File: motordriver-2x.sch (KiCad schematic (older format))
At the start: 442 parts

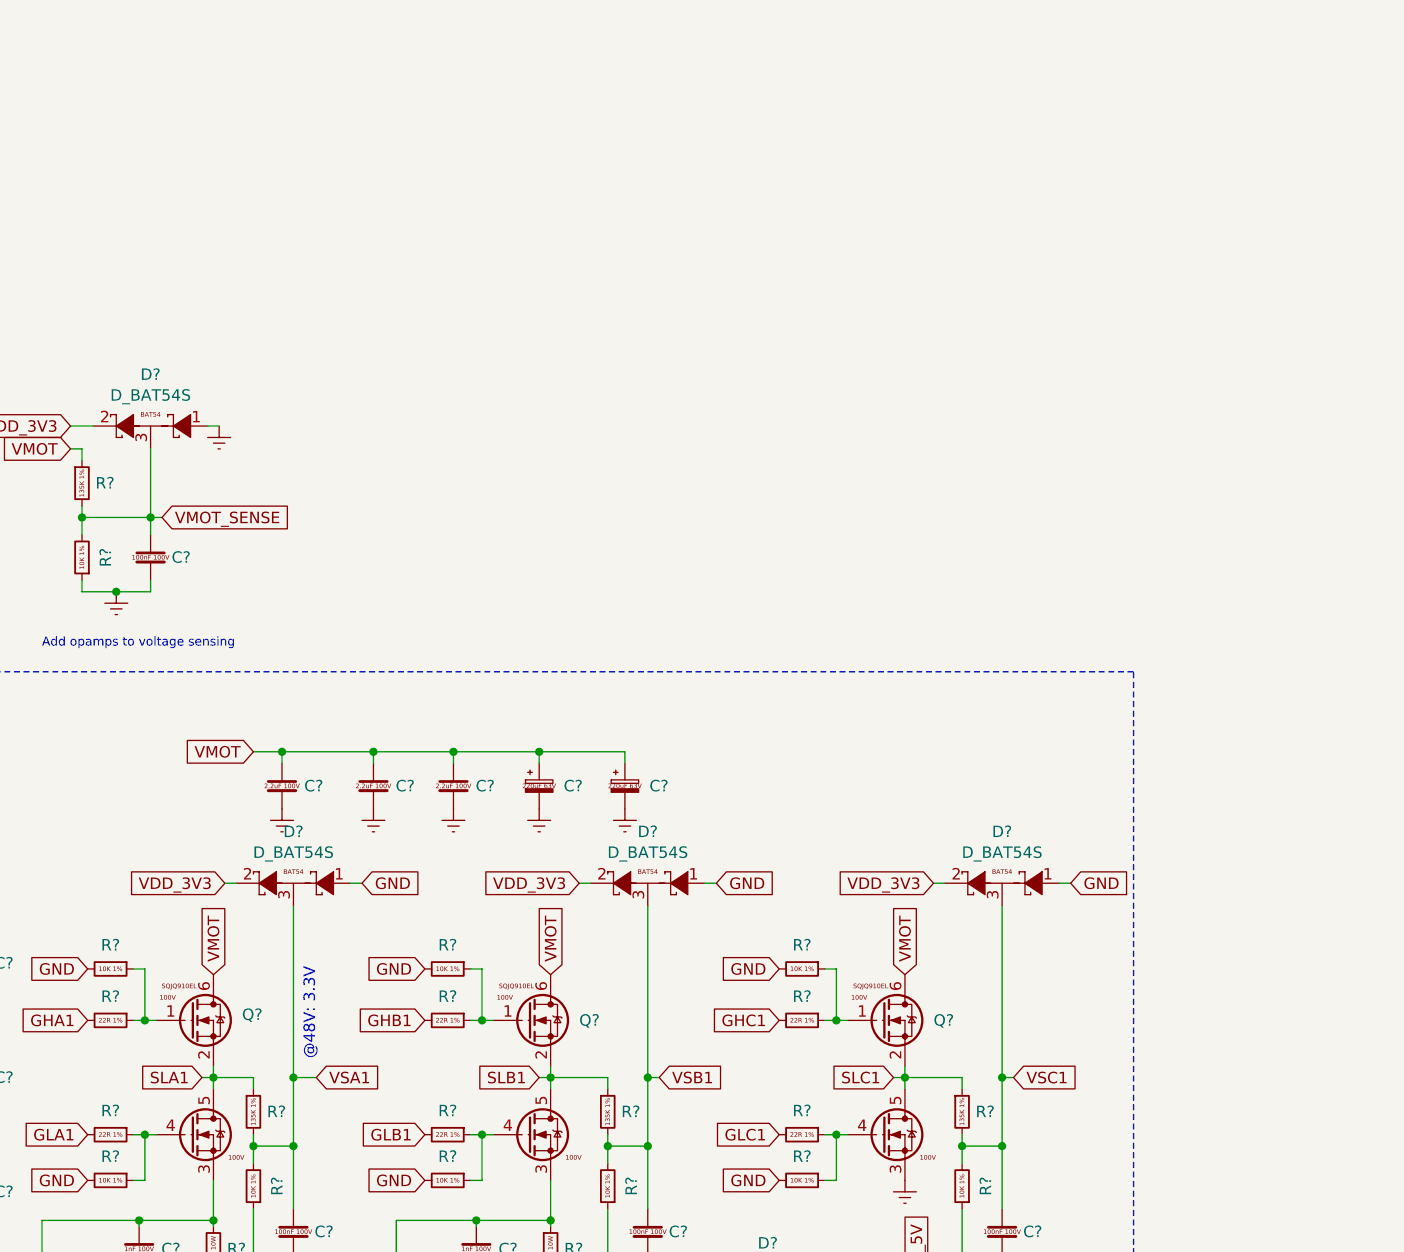
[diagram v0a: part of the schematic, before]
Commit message: add opamps to voltage sensing
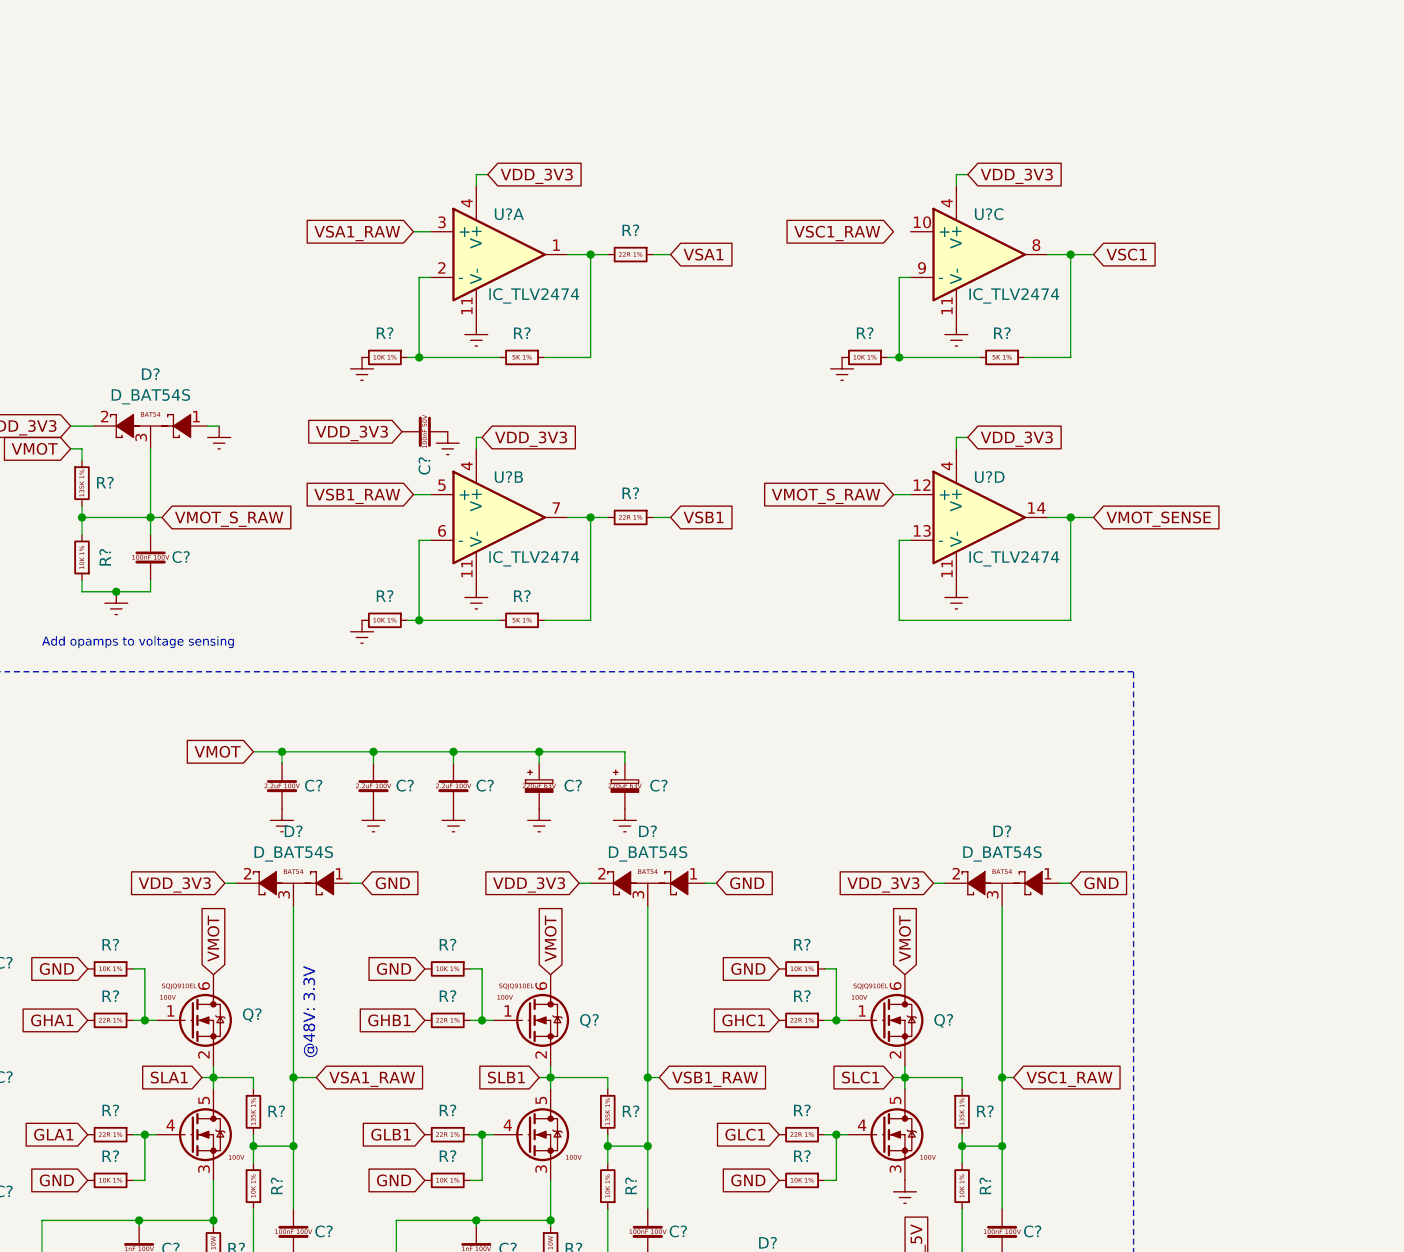
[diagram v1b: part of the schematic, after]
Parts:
- added C?: CAP_100nF_50V_0402, Capacitor_SMD:C_0402_1005Metric, symbol SwEmb:CAP_100nF_50V_0402
- added R? (x2): RES_22R_1%_0402, Resistor_SMD:R_0402_1005Metric, symbol SwEmb:RES_22R_1%_0402
- added R? (x3): RES_5K_1%_0402, Resistor_SMD:R_0402_1005Metric, symbol SwEmb:RES_5K_1%_0402
- added R? (x3): RES_10K_1%_0402, Resistor_SMD:R_0402_1005Metric, symbol SwEmb:RES_10K_1%_0402
- added U? (x4): IC_TLV2474, Package_SO:SOIC-14_3.9x8.7mm_P1.27mm, symbol SwEmb:IC_TLV2474
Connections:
- net labels added: VMOT_S_RAW, VSA1_RAW, VSB1_RAW, VSC1_RAW
- wire segments 1434 -> 1477

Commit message: add preamp for voltage sensing and add UEXT
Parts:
- added C?: CAP_100nF_50V_0402, Capacitor_SMD:C_0402_1005Metric, symbol SwEmb:CAP_100nF_50V_0402
- added C?: CAP_22uF_10V_0805, Capacitor_SMD:C_0805_2012Metric, symbol SwEmb:CAP_22uF_10V_0805
- added D?: D_MM3Z3V3B, Diode_SMD:D_SOD-323F, symbol SwEmb:D_MM3Z3V3B
- added P?: CONN_UEXT, Connector_PinSocket_2.54mm:PinSocket_2x05_P2.54mm_Vertical, symbol SwEmb:CONN_UEXT
- added R? (x19): RES_10K_1%_0402, Resistor_SMD:R_0402_1005Metric, symbol SwEmb:RES_10K_1%_0402
- added R? (x2): RES_22R_1%_0402, Resistor_SMD:R_0402_1005Metric, symbol SwEmb:RES_22R_1%_0402
- added R? (x3): RES_5K_1%_0402, Resistor_SMD:R_0402_1005Metric, symbol SwEmb:RES_5K_1%_0402
- added U? (x4): IC_TLV2474, Package_SO:SOIC-14_3.9x8.7mm_P1.27mm, symbol SwEmb:IC_TLV2474
- added U?: IC_TLV5533, Package_TO_SOT_SMD:SOT-23-5, symbol SwEmb:IC_TLV5533
- R?: symbol SwEmb:RES_10K_1%_0402 -> SwEmb:RES_5K_1%_0402
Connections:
- net labels added: UEXT_CS, UEXT_MISO, UEXT_MOSI, UEXT_PWEN, UEXT_RX, UEXT_SCK, UEXT_SCL, UEXT_SDA, UEXT_TX, VSA2_RAW, VSB2_RAW, VSC2_RAW
- wire segments 1477 -> 1586
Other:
- note added: "Back-EMF ADC Pre-Amp w/ offset"
- note removed: "Add opamps to voltage sensing"
- moved on the sheet: C?, D?, R?, U?, U?A, U?B, U?C, U?D

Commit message: add gpio and connect most pins
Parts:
- removed D?: D_BAT54S, Package_TO_SOT_SMD:SOT-23, symbol SwEmb:D_BAT54S
- added C? (x2): CAP_100nF_50V_0402, Capacitor_SMD:C_0402_1005Metric, symbol SwEmb:CAP_100nF_50V_0402
- added J?: USB_B_Micro, Connector_USB:USB_Micro-B_GCT_USB3076-30-A, symbol SwEmb:USB_B_Micro
- added R? (x2): RES_22R_1%_0402, Resistor_SMD:R_0402_1005Metric, symbol SwEmb:RES_22R_1%_0402
- added U?: IC_USBLC6-2, Package_TO_SOT_SMD:SOT-23-6, symbol SwEmb:IC_USBLC6-2
- added U? (x2): IC_MCP23S17, symbol SwEmb:IC_MCP23S17
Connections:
- net labels added: GPEX0, GPEX1, GPEX2, GPEX3, GPEX4, GPEX5, GPEX6, GPEX7, GPEX_CS, GPEX_INTA, GPEX_INTB, GPEX_RESET, GPIO_CS, GPIO_INTA, GPIO_INTB, GPIO_MISO, GPIO_MOSI, GPIO_RESET, GPIO_SCK, LCD_D4, LCD_D5, LCD_D6, LCD_D7, LCD_EN, LCD_MDATA, LCD_READ, LCD_VO, USB_5V, USB_N, USB_P
- wire segments 1586 -> 1617
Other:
- note added: "Check addresses"
- moved on the sheet: P?

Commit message: update schematic
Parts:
- removed C? (x2): CAP_100nF_50V_0402, Capacitor_SMD:C_0402_1005Metric, symbol SwEmb:CAP_100nF_50V_0402
- removed U?: IC_TXS0108, Package_SO:TSSOP-20_4.4x6.5mm_P0.65mm, symbol SwEmb:IC_TXS0108
- added C? (x5): CAP_2.2uF_16V_0402, Capacitor_SMD:C_0402_1005Metric, symbol SwEmb:CAP_2.2uF_16V_0402
- added C? (x2): CAP_100nF_50V_0402, Capacitor_SMD:C_0402_1005Metric, symbol SwEmb:CAP_100nF_50V_0402
- added P? (x8): CONN_SWITCH, TerminalBlock_4Ucon:TerminalBlock_4Ucon_1x02_P3.50mm_Horizontal, symbol SwEmb:CONN_LED
- added R?: RES_470R_1%_0402, Resistor_SMD:R_0402_1005Metric, symbol SwEmb:RES_470R_1%_0402
- added R? (x8): RES_0R_0402, Resistor_SMD:R_0402_1005Metric, symbol SwEmb:RES_0R_0402
- added U?: IC_LP55231, Package_DFN_QFN:WQFN-24-1EP_4x4mm_P0.5mm_EP2.7x2.7mm, symbol SwEmb:IC_LP55231
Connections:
- net labels added: BLED_EN, BLED_INT, BLED_SCL, BLED_SDA, LCD_D0, LCD_D1, LCD_D2, LCD_D3, LCD_LED
- net labels removed: GPEX0, GPEX1, GPEX2, GPEX3, GPEX4, GPEX5, GPEX6, GPEX7
- wire segments 1617 -> 1703
- no-connect marks 57 -> 53
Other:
- note added: "Button LEDs"
- note added: "LCD"
- note added: "Sw/Ctrl IO"
- note added: "UEXT"
- note removed: "GP/Expansion IO"
- note removed: "Implement industrial digital inputs with 30v tolerance"
- moved on the sheet: C?, P?, U?

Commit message: update annotated schematic
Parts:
- added C70: CAP_100nF_50V_0402, Capacitor_SMD:C_0402_1005Metric, symbol SwEmb:CAP_100nF_50V_0402
- added R39, R55, R61, R65: RES_10mOhm_1%, Resistor_SMD:R_0805_2012Metric, symbol SwEmb:RES_10mOhm_1%
- added R76: RES_22R_1%_0402, Resistor_SMD:R_0402_1005Metric, symbol SwEmb:RES_22R_1%_0402
- added TP10, TP17, TP20, TP21, TP22: Test_Point, TestPoint:TestPoint_Pad_1.0x1.0mm, symbol SwEmb:Test_Point
- added unit 1 of U26
- gave numbers to parts that had none: 503
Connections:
- net BLED_SCL is gone; now on net AP_SCL1: U21.9 (SCL)
- net BLED_SDA is gone; now on net AP_SDA1: U21.8 (SDA)
- net AINPWEN: now also U12.12 (PF2/FMC_A2/I2C2_SMBA)
- net BLED_EN: now also U12.58 (PE7/FMC_D4/FMC_DA4/TIM1_ETR/UART7_RX)
- net BLED_INT: now also U12.67 (PE14/FMC_D11/FMC_DA11/LTDC_CLK/SPI4_MOSI/TIM1_CH4)
- net ENCPWEN1: now also U12.70 (ADC1_EXTI11/ADC2_EXTI11/ADC3_EXTI11/ETH_TX_EN/I2C2_SDA/LTDC_G5/TIM2_CH4/USART3_RX/USB_OTG_HS_ULPI_D4/PB11)
- net ENCPWEN2: now also U12.69 (ETH_RX_ER/I2C2_SCL/I2S2_CK/LTDC_G4/SPI2_SCK/TIM2_CH3/USART3_TX/USB_OTG_HS_ULPI_D3/PB10)
- net GNDREF: now also S2.1 (A1), S2.2 (B1), S2.3 (C1), S2.4 (D1), C70.1, U26.11 (V-)
- net GPEX_CS: now also U12.19 (PF7/ADC3_IN5/FMC_NREG/SAI1_MCLK_B/SPI5_SCK/TIM11_CH1/UART7_TX)
- net GPEX_INTA: now also U12.21 (PF9/ADC3_IN7/DAC_EXTI9/FMC_CD/SAI1_FS_B/SPI5_MOSI/TIM14_CH1)
- net GPEX_INTB: now also U12.22 (PF10/ADC3_IN8/DCMI_D11/FMC_INTR/LTDC_DE)
- net GPEX_RESET: now also U12.20 (PF8/ADC3_IN6/FMC_NIOWR/SAI1_SCK_B/SPI5_MISO/TIM13_CH1)
- net USB_5V: now also R61.2; no longer U22.1 (IN)
- net VDD_3V3: now also C70.2, R65.1, TP22.1, U26.4 (V+); no longer C58.1, U22.5 (OUT)
- net VMOT: now also R39.2, TP10.1; no longer TP11.1, U14.2 (VIN)
- net VMOT_SENSE: now also R76.1
- net VSC1: now also U33.14; no longer U33.8
- net VSC2: now also U35.1; no longer U35.8
- net at S2.5 (D2): now also U13.28 (PA7)
- net at S2.6 (C2): now also U13.27 (PA6)
- net at S2.7 (B2): now also U13.26 (PA5)
- net at S2.8 (A2): now also U13.25 (PA4)
- net at C45.1, P23.1 (VCC), TP16.1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: now also R55.2; no longer C38.1, D14.1 (K), L1.2, R48.1
- net at R134.1, R135.2: now also U33.10 (+); no longer U33.5 (+)
- net at R136.1, R154.2: now also U33.9 (-); no longer U33.6 (-)
- net at R154.1, R162.2: now also U33.8; no longer U33.7
- net at R180.1, R181.2: now also U35.3 (+); no longer U35.10 (+)
- net at R182.1, R194.2: now also U35.2 (-); no longer U35.9 (-)
- net at R90.1, R91.2: now also U26.10 (+); no longer U26.12 (+)
- net at R135.1, R181.1, R98.1: now also U26.8, U26.9 (-); no longer U26.13 (-), U26.14
- net at R111.1, R121.2: now also U26.14; no longer U26.1
- net at R111.2, R96.1: now also U26.13 (-); no longer U26.2 (-)
- net at R94.1, R95.2: now also U26.12 (+); no longer U26.3 (+)
- net at R177.1, R178.2: now also U33.12 (+); no longer U33.10 (+)
- net at R179.1, R193.2: now also U33.13 (-); no longer U33.9 (-)
- net at R88.1, R89.2: now also U26.5 (+); no longer U26.12 (+)
- net at R132.1, R178.1, R95.1: now also U26.6 (-), U26.7; no longer U26.13 (-), U26.14
- net VMOT_S_RAW: no longer names the net of C63.1, D17.3, R68.2, R69.2
- net VMOT_S_RAW: now also U26.3 (+)
- new net: R39.1, TP11.1, U14.2 (VIN)
- new net: C38.1, D14.1 (K), L1.2, R48.1, R55.1, TP17.1
- new net: R61.1, TP20.1, U22.1 (IN)
- new net: C58.1, R65.2, TP21.1, U22.5 (OUT)
- new net: R76.2, U26.1, U26.2 (-)
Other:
- note added: "EtherCAT"
- note added: "GPIO"
- note added: "Supply Voltage Sense"
- note added: "USB"
- note removed: "150mA"
- note removed: "Add current sensing to each supply"
- note removed: "Sw/Ctrl IO"
- note removed: "Use extra inputs for HALL?\nAdd possibility to bypass"
- moved on the sheet: C102, C111, C114, C117, C118, C119, C120, C125, C126, C127, C128, C131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

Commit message: start preliminary pcb layout
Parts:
- D15, D16: Availability (none) -> 110855 In Stock; Description (none) -> Zener Diodes Diode Zener 3.3V 200mW 2%; LifeCycle (none) -> OK; Price (none) -> 0.183 EUR; Vendor (none) -> Mouser
- J2, J3: footprint (none) -> Connector_RJ:RJ45_Tranformer; MFN (none) -> 7499010121A
- P17, P28: Availability (none) -> 11668 In Stock; Description (none) -> Headers & Wire Housings 10P STRT SOLDER TAIL HIGH TEMP; LifeCycle (none) -> OK; Price (none) -> 1.22 EUR; Vendor (none) -> Mouser
- P29, P30, P31, P32, P33, P34, P35, P36: value CONN_SWITCH -> CONN_LED
- P45, P46: footprint TerminalBlock_4Ucon:TerminalBlock_4Ucon_1x03_P3.50mm_Horizontal -> CUSTOM:ANYTEK_7.62mm_2x_3P_32A
- R39, R55, R61, R65: Availability 215652 In Stock -> 7485 In Stock; Description Thick Film Resistors - SMD 1/16watt 22ohms 1% Commercial Use -> Current Sense Resistors - SMD 0.01 ohm 1% 0.5W Current Sense; Price 0.114 EUR -> 0.183 EUR; Vendor (none) -> Mouser
- R69: value RES_10K_1%_0402 -> RES_5K_1%_0402; Availability 1813839 In Stock -> 38996 In Stock; Description Thick Film Resistors - SMD 1/16watt 10Kohms 1% Commercial U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 -> Thick Film Resistors - SMD 5K ohm 1% 50V General Purpose; MPN CRCW040210K0FKEDC -> RC0402FR-075KL; Price 0.114 EUR -> 0.087 EUR
- U13, U5: footprint (none) -> Package_SO:SOIC-28W_7.5x17.9mm_P1.27mm; Availability (none) -> 16730 In Stock; Description (none) -> Interface - I/O Expanders 16bit Input/Output Exp SPI interf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; LifeCycle (none) -> OK; MPN MCP23S17 -> MCP23S17T-E/SO; Price (none) -> 1.19 EUR; Vendor (none) -> Mouser
- U16, U26, U3, U33, U35, U4: Availability 12748 In Stock -> 1390 In Stock; Description Operational Amplifiers - Op Amps Quad -> Precision Amplifiers Quad Lo-Pwr R-to-R Input/Output Op Amp; Price 0.367 EUR -> 2.39 EUR
- U21: Availability (none) -> 19443 In Stock; Description (none) -> LED Lighting Drivers Programmble 9-Output LED Driver; LifeCycle (none) -> OK; Price (none) -> 1.69 EUR; Vendor (none) -> Mouser
- U31, U32: footprint Package_SO_HTSSOP-56-1EP_6.1x14mm_P0.5mm_EP3.61x6.35mm -> CUSTOM:HTSSOP-56-PowerPAD_6.2x14.1mm_P0.5mm_EP3.61x6.35mm
- U6: Availability (none) -> 222317 In Stock; Description (none) -> Multiplexer Switch ICs 8-Channel Analog; LifeCycle (none) -> OK; Price (none) -> 0.533 EUR; Vendor (none) -> Mouser

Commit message: fix footprints
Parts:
- C84, C85: value CAP_2.2uF_100V_1210 -> CAP_2.2uF_16V_0402; footprint Capacitor_SMD:C_1210_3225Metric -> Capacitor_SMD:C_0402_1005Metric; symbol SwEmb:CAP_2.2uF_100V_1210 -> SwEmb:CAP_2.2uF_16V_0402; Availability 12161 In Stock -> 113017 In Stock; Description Multilayer Ceramic Capacitors MLCC - SMD/SMT 2.2uF 100V X7R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 -> Multilayer Ceramic Capacitors MLCC - SMD/SMT 0402 16Vdc 2.2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; MPN HMJ325AB7225KMHT -> GRT155C81C225KE13D; Price 1.00 EUR -> 0.271 EUR
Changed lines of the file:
@@
 DC_CAL1
 $Comp
-L SwEmb:CAP_2.2uF_100V_1210 C84
+L SwEmb:CAP_2.2uF_16V_0402 C84
 U 1 1 5C8F47DA
 P 20425 5600
 F 0 "C84" V 20269 5600 50  0000 C CNN
-F 1 "CAP_2.2uF_100V_1210" H 20435 5520 50  0001 L CNN
-F 2 "Capacitor_SMD:C_1210_3225Metric" H 20875 5750 50  0001 C CNN
-F 3 "https://www.mouser.com/datasheet/2/396/taiyo_yuden_12132018_mlcc11_hq_e-1510082.pdf" H 20435 5670 50  0001 C CNN
-F 4 "HMJ325AB7225KMHT" H 20425 5300 50  0001 C CNN "MPN"
-F 5 "12161 In Stock" H 20425 5600 50  0001 C CNN "Availability"
-F 6 "Multilayer Ceramic Capacitors MLCC - SMD/SMT 2.2uF 100V X7R 10% 1210 Flx AEC-Q200" H 20425 5600 50  0001 C CNN "Description"
+F 1 "CAP_2.2uF_16V_0402" H 20435 5520 50  0001 L CNN
+F 2 "Capacitor_SMD:C_0402_1005Metric" H 20875 5750 50  0001 C CNN
+F 3 "https://www.mouser.com/datasheet/2/281/murata_03122018_GRT_Series-1310174.pdf" H 20435 5670 50  0001 C CNN
+F 4 "GRT155C81C225KE13D" H 20425 5300 50  0001 C CNN "MPN"
+F 5 "113017 In Stock" H 20425 5600 50  0001 C CNN "Availability"
+F 6 "Multilayer Ceramic Capacitors MLCC - SMD/SMT 0402 16Vdc 2.2uF X6S 10%" H 20425 5600 50  0001 C CNN "Description"
 F 7 "OK" H 20425 5600 50  0001 C CNN "LifeCycle"
-F 8 "1.00  EUR" H 20425 5600 50  0001 C CNN "Price"
+F 8 "0.271  EUR" H 20425 5600 50  0001 C CNN "Price"
 F 9 "Mouser" H 4875 575 50  0001 C CNN "Vendor"
 	1    20425 5600
@@
 DC_CAL2
 $Comp
-L SwEmb:CAP_2.2uF_100V_1210 C85
+L SwEmb:CAP_2.2uF_16V_0402 C85
 U 1 1 5CA49E30
 P 20425 9575
 F 0 "C85" V 20269 9575 50  0000 C CNN
-F 1 "CAP_2.2uF_100V_1210" H 20435 9495 50  0001 L CNN
-F 2 "Capacitor_SMD:C_1210_3225Metric" H 20875 9725 50  0001 C CNN
-F 3 "https://www.mouser.com/datasheet/2/396/taiyo_yuden_12132018_mlcc11_hq_e-1510082.pdf" H 20435 9645 50  0001 C CNN
-F 4 "HMJ325AB7225KMHT" H 20425 9275 50  0001 C CNN "MPN"
-F 5 "12161 In Stock" H 20425 9575 50  0001 C CNN "Availability"
-F 6 "Multilayer Ceramic Capacitors MLCC - SMD/SMT 2.2uF 100V X7R 10% 1210 Flx AEC-Q200" H 20425 9575 50  0001 C CNN "Description"
+F 1 "CAP_2.2uF_16V_0402" H 20435 9495 50  0001 L CNN
+F 2 "Capacitor_SMD:C_0402_1005Metric" H 20875 9725 50  0001 C CNN
+F 3 "https://www.mouser.com/datasheet/2/281/murata_03122018_GRT_Series-1310174.pdf" H 20435 9645 50  0001 C CNN
+F 4 "GRT155C81C225KE13D" H 20425 9275 50  0001 C CNN "MPN"
+F 5 "113017 In Stock" H 20425 9575 50  0001 C CNN "Availability"
+F 6 "Multilayer Ceramic Capacitors MLCC - SMD/SMT 0402 16Vdc 2.2uF X6S 10%" H 20425 9575 50  0001 C CNN "Description"
 F 7 "OK" H 20425 9575 50  0001 C CNN "LifeCycle"
-F 8 "1.00  EUR" H 20425 9575 50  0001 C CNN "Price"
+F 8 "0.271  EUR" H 20425 9575 50  0001 C CNN "Price"
 F 9 "Mouser" H 4875 575 50  0001 C CNN "Vendor"
 	1    20425 9575

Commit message: add break resistor circuit and simulation
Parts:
- added D?: D_CDBC5100, Diode_SMD:D_SMC, symbol SwEmb:D_CDBC5100
- added D?: D_STPS41H100, Package_TO_SOT_SMD:TO-263-2, symbol SwEmb:D_STPS41H100
- added D? (x2): D_BAT54, Diode_SMD:D_SOD-123, symbol SwEmb:D_BAT54
- added P?: CONN_BRKRES, TerminalBlock_4Ucon:TerminalBlock_4Ucon_1x02_P3.50mm_Horizontal, symbol SwEmb:CONN_BRKRES
- added Q?: Q_NMOS_BUK9875, Package_TO_SOT_SMD:SOT-223, symbol SwEmb:Q_NMOS_BUK9875
- added Q?: Q_PNP_BC856, Package_TO_SOT_SMD:SOT-23, symbol SwEmb:Q_PNP_BC856
- added R?: RES_10K_1%_0402, Resistor_SMD:R_0402_1005Metric, symbol SwEmb:RES_10K_1%_0402
- added R? (x2): RES_135K_1%_0402, Resistor_SMD:R_0402_1005Metric, symbol SwEmb:RES_135K_1%_0402
- added TP?: Test_Point, TestPoint:TestPoint_Pad_1.0x1.0mm, symbol SwEmb:Test_Point
- U13, U5: Availability 16730 In Stock -> 12705 In Stock; Price 1.19 EUR -> 1.14 EUR
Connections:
- net GNDREF: now also D?.2, Q?.3 (S), R?.2
- net VMOT: now also D?.2, P?.1 (BR), Q?.2 (E); no longer C15.1, D9.1 (K), P18.1 (VCC), R39.2, TP10.1
- new net: C15.1, D?.1 (K), R39.2, TP10.1
- new net: D?.1, Q?.1 (G), R?.1, R?.1, TP?.1
- new net: P?.2 (BR), Q?.2 (D), Q?.4 (D)
- new net: D?.1, R?.1
- new net: D?.2, Q?.1 (B)
- new net: Q?.3 (C), R?.2
- new net BREAK: D9.1 (K), D?.1, D?.2 (A), D?.3, P18.1 (VCC), R?.2
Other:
- note added: "0-3V"
- note added: "Brake Resistor"
- note added: "VMOT"
